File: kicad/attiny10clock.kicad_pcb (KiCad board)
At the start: 2 copper layers, 46 parts, among them J1 USB_B, SW1 SW_DIP_x01, SW2 SW_DIP_x01, SW3 SW_DIP_x01, SW4 SW_DIP_x01, SW5 SW_DIP_x01, U1 ATtiny10-TS, U2 74HC595, U3 74HC595, U4 74LS247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

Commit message: Rev 3 of schematic, start pcb
also new code rev
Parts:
- removed C10, C9: 100n, Capacitor_SMD:C_0805_2012Metric_Pad1.15x1.40mm_HandSolder
- removed R6: 270, Resistor_SMD:R_1210_3225Metric_Pad1.42x2.65mm_HandSolder
- removed REF**: MountingHole_3.2mm_M3, MountingHole:MountingHole_3.2mm_M3
- removed U6, U7: 74LS247, Package_SO:SOIC-16_3.9x9.9mm_P1.27mm
- added F1: 500ma, Fuse:Fuse_1206_3216Metric_Pad1.42x1.75mm_HandSolder, F.Cu at (108.7, 71.9)
- added J2: Conn_02x04_Odd_Even, Connector_PinHeader_2.54mm:PinHeader_2x04_P2.54mm_Vertical, F.Cu at (129.7, 36.5)
- C1, C12, C3, C6, C7, J1, L1, R7, SW1, SW2, SW3, SW4, SW5, U8: moved to F.Cu
- U2, U3: value 74HC595 -> NPIC6C595; footprint Package_SO:SOIC-16_3.9x9.9mm_P1.27mm -> Package_SO:TSSOP-16_4.4x5mm_P0.65mm
- U4, U5: value 74LS247 -> NPIC6C595; footprint Package_SO:SOIC-16_3.9x9.9mm_P1.27mm -> Package_SO:TSSOP-16_4.4x5mm_P0.65mm
- X1: footprint Oscillator:Oscillator_SMD_Fordahl_DFAS15-4Pin_5.0x3.2mm -> random_stuff:ASFLK
- moved C3 95.7 mm to (137.6, 62.5), turned to 0 degrees
- moved U5 89.4 mm to (148.8, 37.6), turned to 0 degrees
- moved C12 83.1 mm to (137.8, 38.9), turned to 0 degrees
- moved SW1 81.8 mm to (139.4, 53.2), turned to 0 degrees
- moved C1 81.3 mm to (148.8, 42.4), turned to 0 degrees
- moved C13 80.1 mm to (148.8, 45.3)
- moved C7 78.3 mm to (144.1, 52.4), turned to 0 degrees
- moved C11 77.9 mm to (148.8, 48.3), turned to 0 degrees
- moved R5 77.8 mm to (148.7, 53.5), turned to 0 degrees
- moved C6 76.7 mm to (130.6, 51.2), turned to 0 degrees
- moved R1 74.3 mm to (148.7, 51.0), turned to 0 degrees
- moved R9 73.5 mm to (143.9, 55.1), turned to 0 degrees
- moved SW2 70.5 mm to (144.1, 46.0), turned to 0 degrees
- moved J1 70.2 mm to (111.3, 41.7), turned to 0 degrees
- moved R8 68.5 mm to (142.2, 59.3), turned to 0 degrees
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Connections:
- D1 pad 1: GND -> Net-(D1-Pad1)
- D1 pad 2: Net-(D1-Pad2) -> /2v
- D2 pad 1: GND -> Net-(D1-Pad1)
- D2 pad 2: Net-(D1-Pad2) -> /2v
- J1 pad 1: Net-(J1-Pad1) -> Net-(F1-Pad2)
- SW1 pad 1: Net-(J1-Pad1) -> Net-(F1-Pad1)
- U1 pad 1: Net-(U1-Pad1) -> Net-(J2-Pad1)
- U1 pad 3: Net-(U1-Pad3) -> Net-(J2-Pad3)
- U1 pad 6: Net-(C2-Pad1) -> Net-(J2-Pad7)
- U2 pad 1: /minha -> +5V
- U2 pad 10: +5V -> Net-(J2-Pad4)
- U2 pad 11: Net-(U1-Pad3) -> Net-(D3-Pad1)
- U2 pad 12: Net-(U1-Pad3) -> Net-(D3-Pad9)
- U2 pad 13: GND -> Net-(D3-Pad10)
- U2 pad 14: Net-(U1-Pad1) -> (no net)
- U2 pad 15: (no net) -> Net-(J2-Pad4)
- U2 pad 16: +5V -> GND
- U2 pad 2: /minhc -> Net-(J2-Pad2)
- U2 pad 3: /minhb -> Net-(D3-Pad7)
- U2 pad 4: /minla -> Net-(D3-Pad6)
- U2 pad 5: /minld -> Net-(D3-Pad4)
- U2 pad 6: /minlc -> Net-(D3-Pad2)
- U2 pad 7: /minlb -> +5V
- U3 pad 1: /hourha -> +5V
- U3 pad 10: +5V -> Net-(J2-Pad4)
- U3 pad 11: Net-(U1-Pad3) -> Net-(D4-Pad1)
- U3 pad 12: Net-(U1-Pad3) -> Net-(D4-Pad9)
- U3 pad 13: GND -> Net-(D4-Pad10)
- U3 pad 14: Net-(U2-Pad9) -> Net-(D1-Pad1)
- U3 pad 15: (no net) -> Net-(J2-Pad4)
- U3 pad 16: +5V -> GND
- U3 pad 2: /hourhb -> Net-(U2-Pad9)
- U3 pad 3: /hourla -> Net-(D4-Pad7)
- U3 pad 4: /hourld -> Net-(D4-Pad6)
- U3 pad 5: /hourlc -> Net-(D4-Pad4)
- U3 pad 6: /hourlb -> Net-(D4-Pad2)
- U3 pad 7: Net-(R6-Pad2) -> +5V
- U3 pad 9: (no net) -> Net-(U3-Pad9)
- U4 pad 1: /minlb -> +5V
- U4 pad 10: Net-(D3-Pad2) -> Net-(J2-Pad4)
- U4 pad 11: Net-(D3-Pad4) -> Net-(D5-Pad1)
- U4 pad 12: Net-(D3-Pad6) -> Net-(D5-Pad9)
- U4 pad 13: Net-(D3-Pad7) -> Net-(D5-Pad10)
- U4 pad 14: Net-(D3-Pad10) -> (no net)
- U4 pad 15: Net-(D3-Pad9) -> Net-(J2-Pad4)
- U4 pad 16: +5V -> GND
- U4 pad 2: /minlc -> Net-(U3-Pad9)
- U4 pad 3: +5V -> Net-(D5-Pad7)
- U4 pad 4: (no net) -> Net-(D5-Pad6)
- U4 pad 5: +5V -> Net-(D5-Pad4)
- U4 pad 6: /minld -> Net-(D5-Pad2)
- U4 pad 7: /minla -> +5V
- U4 pad 9: Net-(D3-Pad1) -> Net-(U4-Pad9)
- U5 pad 1: /minhb -> +5V
- U5 pad 10: Net-(D4-Pad2) -> Net-(J2-Pad4)
- U5 pad 11: Net-(D4-Pad4) -> Net-(D6-Pad1)
- U5 pad 12: Net-(D4-Pad6) -> Net-(D6-Pad9)
- U5 pad 13: Net-(D4-Pad7) -> Net-(D6-Pad10)
- U5 pad 14: Net-(D4-Pad10) -> (no net)
- U5 pad 15: Net-(D4-Pad9) -> Net-(J2-Pad4)
- U5 pad 16: +5V -> GND
- U5 pad 2: /minhc -> Net-(U4-Pad9)
- U5 pad 3: +5V -> Net-(D6-Pad7)
- U5 pad 4: (no net) -> Net-(D6-Pad6)
- U5 pad 5: +5V -> Net-(D6-Pad4)
- U5 pad 6: GND -> Net-(D6-Pad2)
- U5 pad 7: /minha -> +5V
- U5 pad 9: Net-(D4-Pad1) -> (no net)
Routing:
- net +5V: track 331.6 -> 6.19 mm, vias 11 -> 0
- net /2v: track 205.2 -> 0.00 mm, vias 5 -> 0
- net GND: track 103.2 -> 0.00 mm, vias 13 -> 0
- net Net-(U1-Pad3): track 54.4 -> 0.00 mm
- net Net-(U2-Pad9): track 51.6 -> 0.00 mm
- net Net-(R7-Pad1): track 36.0 -> 0.00 mm
- net Net-(U1-Pad1): track 35.8 -> 0.00 mm
- net Net-(C2-Pad1): track 33.2 -> 0.00 mm, vias 2 -> 0
- net /hourlb: track 31.0 -> 0.00 mm
- net /hourlc: track 29.8 -> 0.00 mm
- net /minlb: track 25.8 -> 0.00 mm
- net /minhb: track 25.1 -> 0.00 mm
- net /hourld: track 24.5 -> 0.00 mm
- net /minlc: track 23.7 -> 0.00 mm
- net /hourla: track 23.3 -> 0.00 mm
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- removed copper zone on B.Cu, net GND
- removed copper zone on F.Cu, net GND
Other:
- net class Default: clearance 0.25 -> 0.2; trace_width 0.5 -> 0.3; via_dia 1.4 -> 0.8
- rule trace_clearance: 0.25 -> 0.2
- board text removed: "ATtiny10 Clock V1"

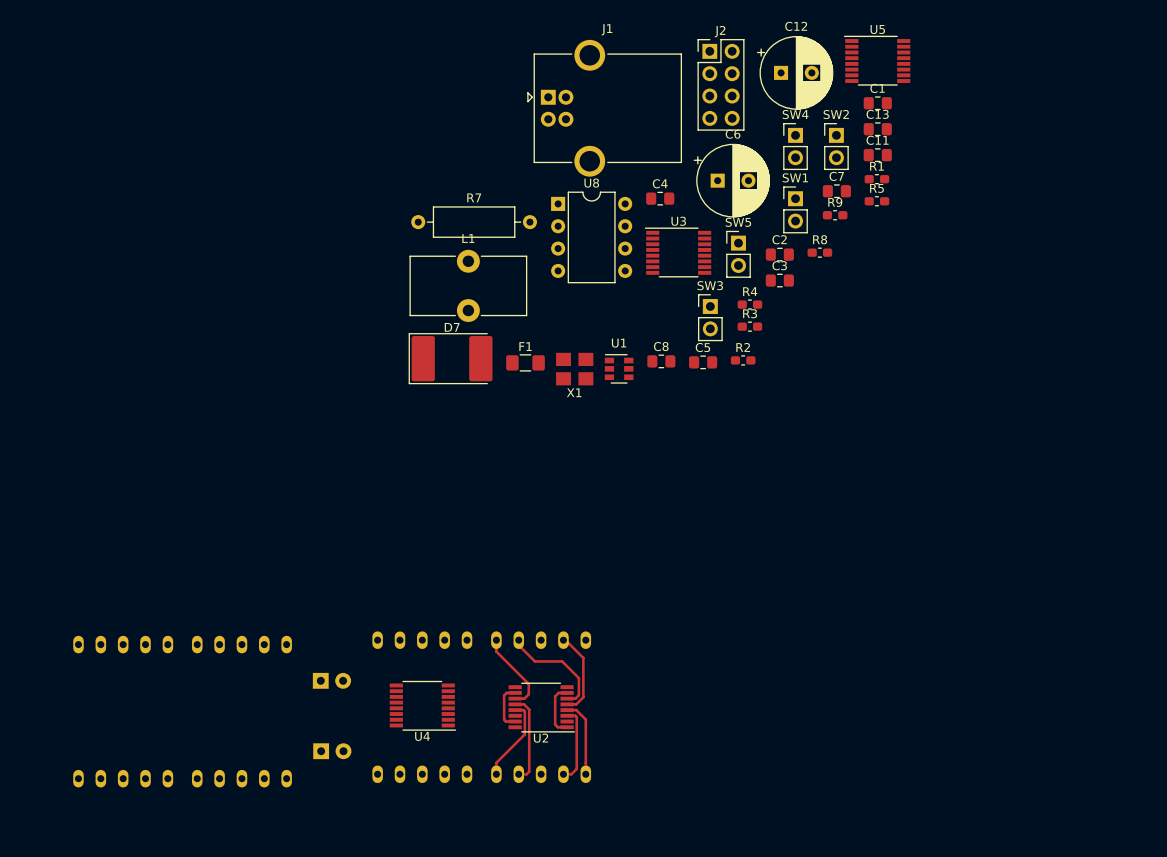
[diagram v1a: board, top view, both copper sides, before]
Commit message: Úse another buck converter
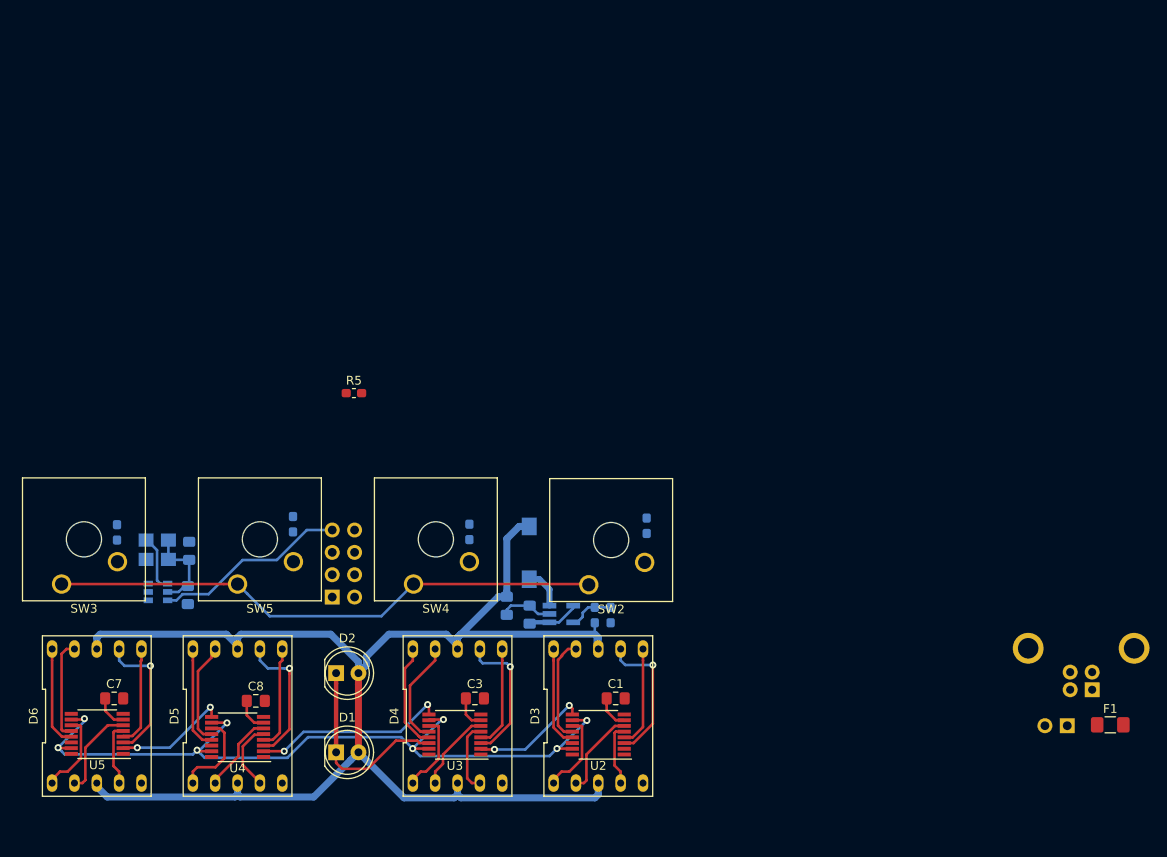
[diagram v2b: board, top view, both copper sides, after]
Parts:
- removed C11: 470p, Capacitor_SMD:C_0805_2012Metric_Pad1.15x1.40mm_HandSolder
- removed C12: 180u, Capacitor_THT:CP_Radial_D8.0mm_P3.50mm
- removed C13: 100n, Capacitor_SMD:C_0805_2012Metric_Pad1.15x1.40mm_HandSolder
- removed C2: 1u, Capacitor_SMD:C_0805_2012Metric_Pad1.15x1.40mm_HandSolder
- removed D7: D_Schottky, Diode_SMD:D_3220_8050Metric_Pad2.65x5.15mm_HandSolder
- removed R8: 5k6, Resistor_SMD:R_0603_1608Metric_Pad1.05x0.95mm_HandSolder
- removed R9: 3k3, Resistor_SMD:R_0603_1608Metric_Pad1.05x0.95mm_HandSolder
- removed U8: MC34063AP, Package_DIP:DIP-8_W7.62mm
- added C9: 22u, Capacitor_SMD:C_0805_2012Metric_Pad1.15x1.40mm_HandSolder, B.Cu at (106.6, 99.5)
- added R6: 27k, Resistor_SMD:R_0603_1608Metric_Pad1.05x0.95mm_HandSolder, B.Cu at (116.6, 100.5)
- added U6: RT8097AHGB, Package_TO_SOT_SMD:SOT-23-5_HandSoldering, B.Cu at (112.8, 100.4)
- C4, C5, J1, J2, SW1, U1, X1: moved to B.Cu
- C6: value 100u -> 22u; footprint Capacitor_THT:CP_Radial_D8.0mm_P3.50mm -> Capacitor_SMD:C_0805_2012Metric_Pad1.15x1.40mm_HandSolder; moved to B.Cu
- D1, D2, D3, D4, D5, D6: moved to F.Cu
- L1: value 100u -> 1.5u; footprint Inductor_THT:L_Toroid_Vertical_L13.0mm_W6.5mm_P5.60mm -> Inductor_SMD:L_Wuerth_WE-PD-Typ-7345; moved to B.Cu
- R1: value 100 -> 22k; moved to B.Cu
- R2: value 300 -> 10k; moved to B.Cu
- R3: value 1k -> 3k9; moved to B.Cu
- R4: value 3k -> 1k2; moved to B.Cu
- R5: value 1k -> 10k
- R7: value 150m -> 12k; footprint Resistor_THT:R_Axial_DIN0309_L9.0mm_D3.2mm_P12.70mm_Horizontal -> Resistor_SMD:R_0603_1608Metric_Pad1.05x0.95mm_HandSolder; moved to B.Cu
- SW2, SW3, SW4, SW5: footprint Connector_PinHeader_2.54mm:PinHeader_1x02_P2.54mm_Vertical -> Button_Switch_Keyboard:SW_Cherry_MX_1.00u_Plate
- moved U5 117.1 mm to (60.0, 114.0), turned to 180 degrees
- moved C7 100.3 mm to (62.0, 110.0)
- moved J1 91.4 mm to (173.1, 109.0), turned to 90 degrees
- moved SW3 80.2 mm to (56.0, 97.0), turned to 180 degrees
- moved F1 78.2 mm to (175.2, 113.0)
- moved J2 75.4 mm to (86.8, 98.5)
- moved C1 73.9 mm to (119.0, 110.0)
- moved R2 73.8 mm to (62.3, 91.1), turned to 270 degrees
- moved C4 70.1 mm to (70.3, 98.2), turned to 270 degrees
- moved SW5 68.9 mm to (76.0, 97.0), turned to 180 degrees
- moved SW1 67.4 mm to (170.3, 113.1), turned to 90 degrees
- moved SW4 67.0 mm to (96.0, 97.0), turned to 180 degrees
- moved R5 63.3 mm to (89.2, 75.3)
- moved C5 62.2 mm to (70.5, 93.2), turned to 90 degrees
- moved U3 60.4 mm to (100.7, 114.1), turned to 180 degrees
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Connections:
- net /2v renamed 2v
- net Net-(C2-Pad1) renamed btn_in
- net Net-(J2-Pad2) renamed ser_in
- net Net-(J2-Pad4) renamed ser_clk
- net Net-(U1-Pad4) renamed clk
- R7 pad 2: +5V -> GND
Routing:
- net 2v: track 0.00 -> 165.8 mm
- net +5V: track 6.19 -> 94.5 mm
- net ser_clk: track 5.46 -> 92.1 mm, vias 0 -> 8
- net Net-(D1-Pad1): track 0.00 -> 22.5 mm
- net Net-(U3-Pad9): track 0.00 -> 22.0 mm, vias 0 -> 2
- net Net-(J2-Pad7): track 0.00 -> 22.0 mm
- net Net-(D4-Pad7): track 0.00 -> 15.8 mm, vias 0 -> 1
- net Net-(D6-Pad7): track 0.00 -> 15.7 mm, vias 0 -> 1
- net Net-(D5-Pad7): track 0.00 -> 15.7 mm, vias 0 -> 1
- net Net-(U2-Pad9): track 0.00 -> 13.3 mm, vias 0 -> 2
- net Net-(U4-Pad9): track 0.00 -> 13.0 mm, vias 0 -> 2
- net Net-(D4-Pad10): track 0.00 -> 12.1 mm
- net Net-(D4-Pad9): track 0.00 -> 12.0 mm
- net Net-(D5-Pad6): track 0.00 -> 11.8 mm
- net Net-(D5-Pad10): track 0.00 -> 11.8 mm
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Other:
- net class led added: clearance 0.2, trace_width 0.5, via_dia 0.8, via_drill 0.4

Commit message: Use new micro usb + more routing
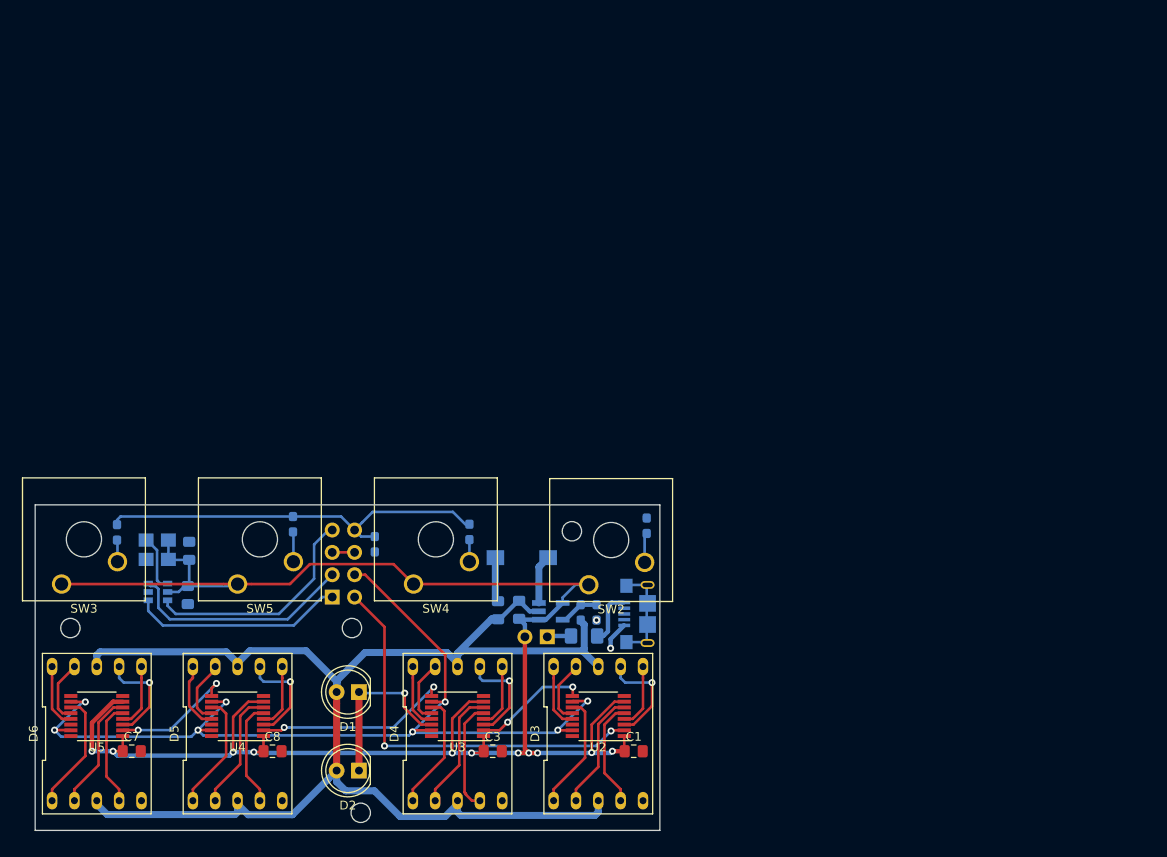
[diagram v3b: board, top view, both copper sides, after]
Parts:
- added H1: MountingHole, MountingHole:MountingHole_2.2mm_M2, F.Cu at (114.0, 91.0)
- added H2: MountingHole, MountingHole:MountingHole_2.2mm_M2, F.Cu at (57.0, 102.0)
- added H3: MountingHole, MountingHole:MountingHole_2.2mm_M2, F.Cu at (90.0, 123.0)
- added H4: MountingHole, MountingHole:MountingHole_2.2mm_M2, F.Cu at (89.0, 102.0)
- F1, R5: moved to B.Cu
- J1: value USB_B -> USB_B_Micro; footprint Connector_USB:USB_B_OST_USB-B1HSxx_Horizontal -> random_stuff:USB_MICRO_10118193-0001LF
- moved F1 60.6 mm to (115.4, 102.9)
- moved SW1 60.0 mm to (111.2, 103.0)
- moved J1 51.3 mm to (122.6, 100.4), turned to 270 degrees
- moved R5 17.3 mm to (91.6, 92.5), turned to 90 degrees
- moved D2 11.4 mm to (89.8, 118.2), turned to 180 degrees
- moved D1 7.33 mm to (89.8, 109.3), turned to 180 degrees
- moved C1 6.34 mm to (121.0, 116.0)
- moved C3 6.33 mm to (105.0, 116.0)
- moved C7 6.32 mm to (64.0, 116.0)
- moved C8 6.03 mm to (80.0, 116.0)
- moved U4 2.38 mm to (76.0, 112.0)
- moved U3 2.12 mm to (101.0, 112.0)
- moved U2 2.10 mm to (117.0, 112.0)
- moved U5 2.03 mm to (60.0, 112.0)
- moved D3 2.00 mm to (117.0, 114.0)
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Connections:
- J1 pad 4: GND -> (no net)
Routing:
- net +5V: track 94.5 -> 209.7 mm, vias 0 -> 11
- net ser_in: track 0.00 -> 46.3 mm, vias 0 -> 2
- net btn_in: track 0.00 -> 45.4 mm
- net Net-(J2-Pad3): track 0.00 -> 26.1 mm
- net Net-(J2-Pad1): track 0.00 -> 24.1 mm
- net ser_clk: track 92.1 -> 111.0 mm
- net Net-(J1-Pad6): track 0.00 -> 11.5 mm
- net GND: track 6.02 -> 12.7 mm, vias 0 -> 2
- net Net-(F1-Pad2): track 0.00 -> 6.24 mm
- net Net-(D3-Pad4): track 7.15 -> 12.2 mm
- net Net-(D5-Pad2): track 9.10 -> 13.8 mm
- net Net-(D4-Pad9): track 12.0 -> 7.30 mm
- net Net-(D6-Pad4): track 7.20 -> 11.9 mm
- net Net-(D4-Pad10): track 12.1 -> 7.48 mm
- net Net-(D3-Pad9): track 12.0 -> 7.36 mm
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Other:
- board outline added: 71 x 37 mm

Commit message: Finalize rev 2 pcb
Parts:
- removed H3: MountingHole, MountingHole:MountingHole_2.2mm_M2
- added 2V: TestPoint, TestPoint:TestPoint_Pad_D2.0mm, F.Cu at (114.2, 100.2)
- C1, C3, C7, C8, D1, D2, D3, D4, D5, D6, SW2, SW3, SW4, SW5, U2, U3, U4, U5: moved to B.Cu
- C4, C5, C6, C9, F1, J1, J2, L1, R1, R2, R3, R4, R5, R6, R7, SW1, U1, U6, X1: moved to F.Cu
- H1, H2, H4: value MountingHole -> MountingHole_Pad; footprint MountingHole:MountingHole_2.2mm_M2 -> MountingHole:MountingHole_2.2mm_M2_Pad
- moved SW3 101.0 mm to (157.0, 96.5), turned to 0 degrees
- moved D6 93.0 mm to (153.0, 113.5), turned to 180 degrees
- moved U5 93.0 mm to (153.0, 111.5), turned to 0 degrees
- moved R2 88.7 mm to (151.0, 90.4)
- moved C7 85.1 mm to (149.0, 115.5), turned to 180 degrees
- moved X1 79.2 mm to (146.1, 92.7), turned to 0 degrees
- moved U1 79.1 mm to (146.1, 97.4), turned to 180 degrees
- moved H2 72.8 mm to (127.0, 122.0)
- moved C4 72.3 mm to (142.7, 97.8)
- moved C5 72.0 mm to (142.5, 92.7)
- moved D5 61.0 mm to (137.0, 113.5), turned to 180 degrees
- moved SW5 61.0 mm to (137.0, 96.5), turned to 0 degrees
- moved U4 61.0 mm to (137.0, 111.5), turned to 0 degrees
- moved C8 53.1 mm to (133.0, 115.5), turned to 180 degrees
- moved R4 48.7 mm to (131.0, 90.4)
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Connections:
- H1 pad 1: (no net) -> GND
- H2 pad 1: (no net) -> GND
- H4 pad 1: (no net) -> GND
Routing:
- net GND: track 12.7 -> 87.7 mm, vias 2 -> 5
- net btn_in: track 45.4 -> 62.2 mm
- net 2v: track 161.6 -> 171.6 mm
- net Net-(U2-Pad9): track 13.2 -> 16.8 mm
- net +5V: track 209.7 -> 212.5 mm
- net ser_clk: track 111.0 -> 112.5 mm
- net Net-(R4-Pad2): track 3.41 -> 2.80 mm
- net Net-(R1-Pad2): track 3.39 -> 2.85 mm
- added copper zone on B.Cu, net GND
- added copper zone on F.Cu, net GND
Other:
- board text added: "."
- board text added: "ATtiny10 Clock V2 Anton Lööf 2021"
- board text added: "JLCJLCJLCJLC"
- board text added: "io3 gnd io1 io0"
- board text added: "power"
